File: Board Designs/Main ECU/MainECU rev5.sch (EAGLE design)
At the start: 164 parts, among them X1 CONNECTOR-37, X2 CONNECTOR-4AUTOSPORT, X3 CONNECTOR-4NANO-FIT-VERTICAL-4, X4 CONNECTOR-4NANO-FIT-VERTICAL-4

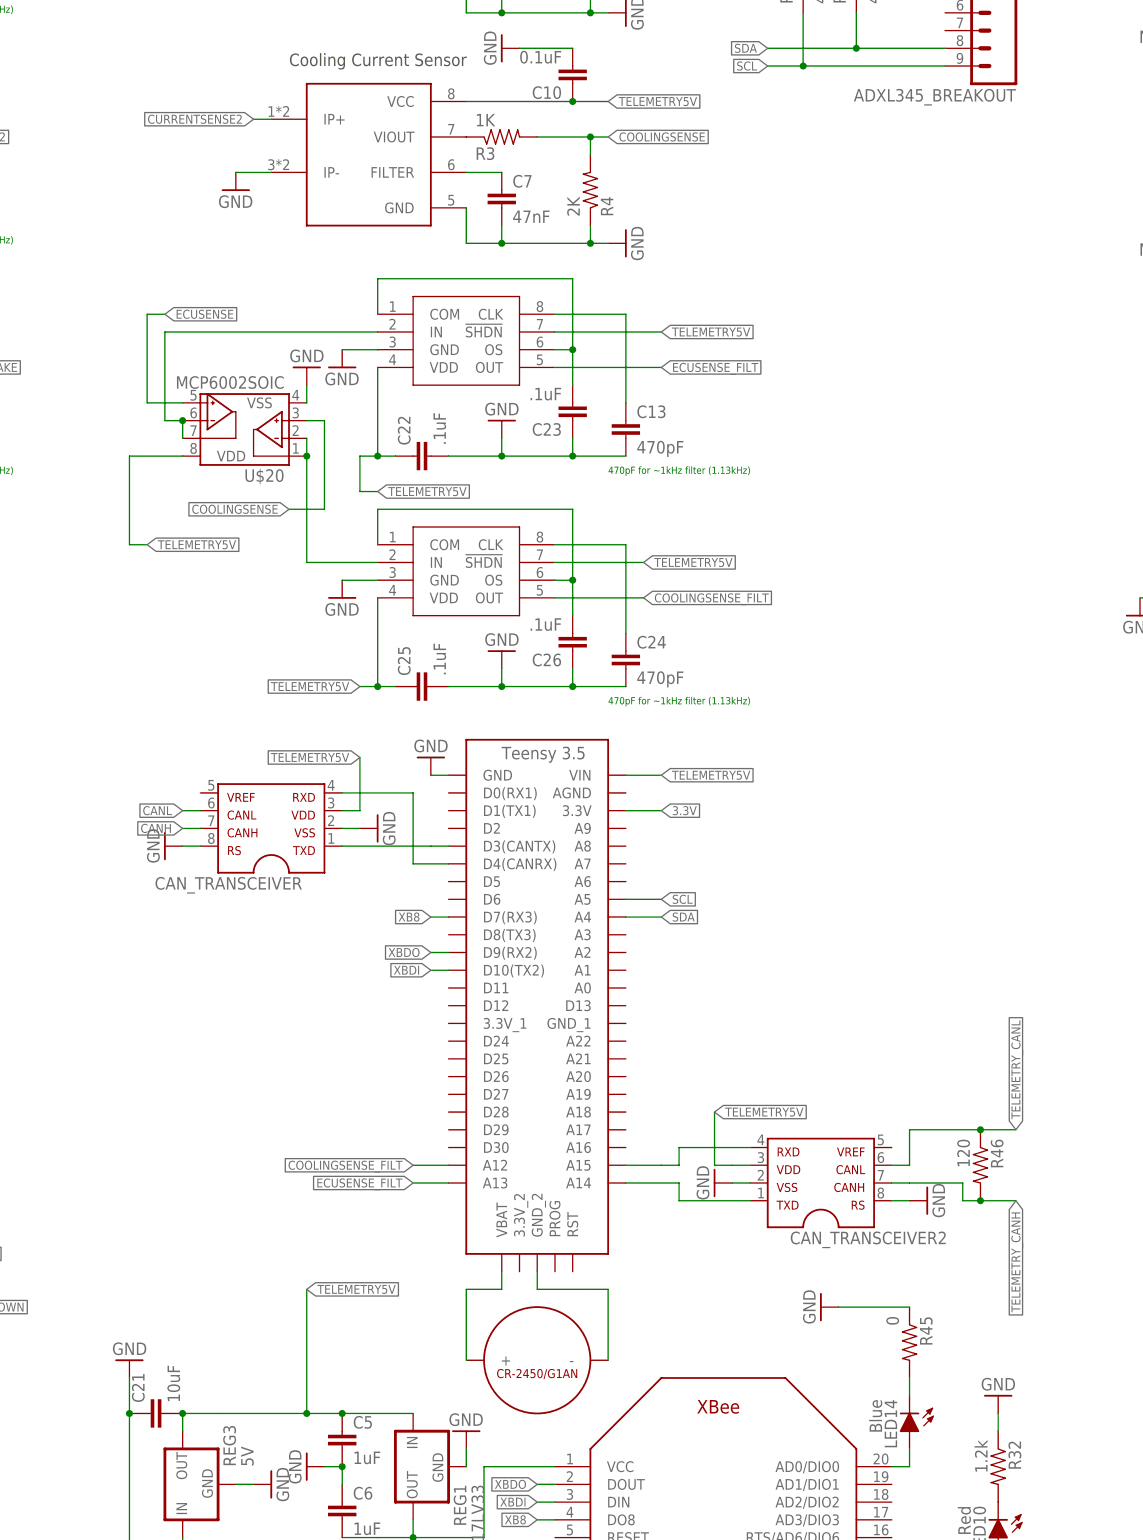
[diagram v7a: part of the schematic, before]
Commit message: Main ECU rev5: Add MTK3339 GPS breakout
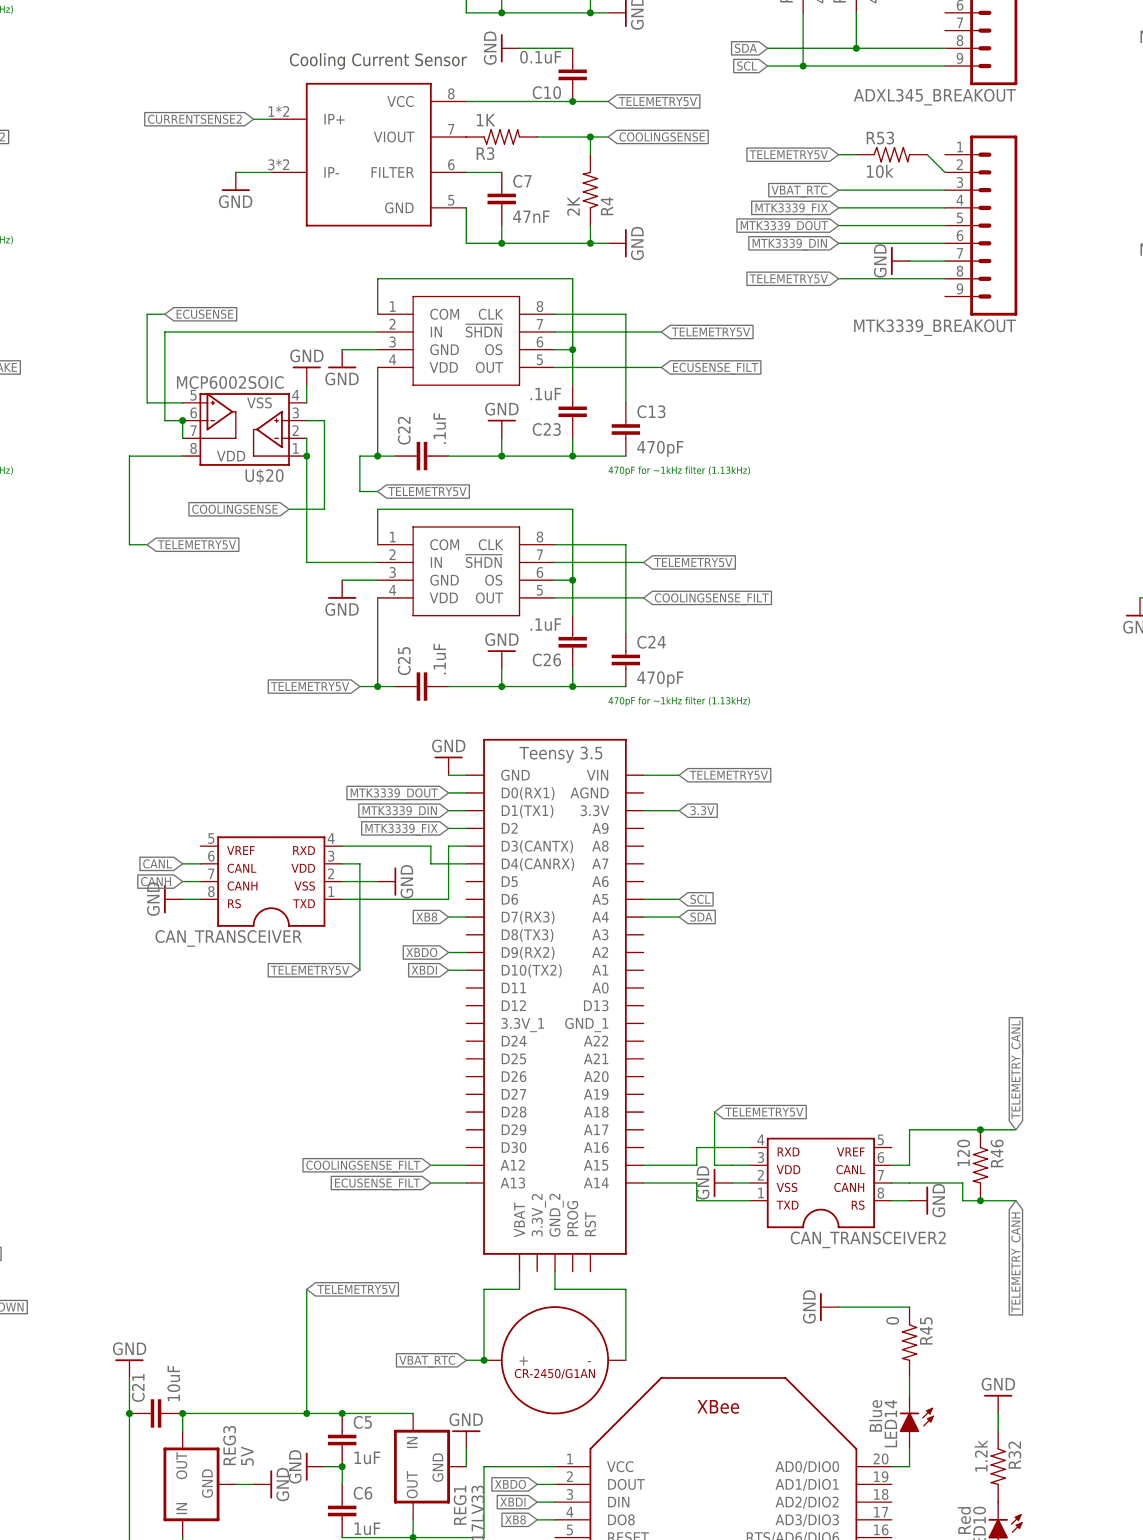
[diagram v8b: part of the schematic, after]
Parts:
- added MTK3339_BREAKOUT: (no value), HyTechDevices:M09
- added R53: 10k, HyTechDevices:RESISTOR0805-RES
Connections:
- removed net N$60: U$16.+, U$2.VBAT
- new net MTK3339_DIN: MTK3339_BREAKOUT.6, U$2.D1(TX1)
- new net MTK3339_DOUT: MTK3339_BREAKOUT.5, U$2.D0(RX1)
- new net MTK3339_FIX: MTK3339_BREAKOUT.4, U$2.D2
- new net N$7: MTK3339_BREAKOUT.2, R53.2
- new net VBAT_RTC: MTK3339_BREAKOUT.3, U$16.+, U$2.VBAT
- net GND: now also MTK3339_BREAKOUT.7
- net TELEMETRY5V: now also MTK3339_BREAKOUT.8, R53.1
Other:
- moved on the sheet: CAN_TRANSCEIVER
